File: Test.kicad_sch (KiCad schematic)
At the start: 17 parts, among them Q1 DMTH10H015LK3-13, U1 ${SIM.PARAMS}

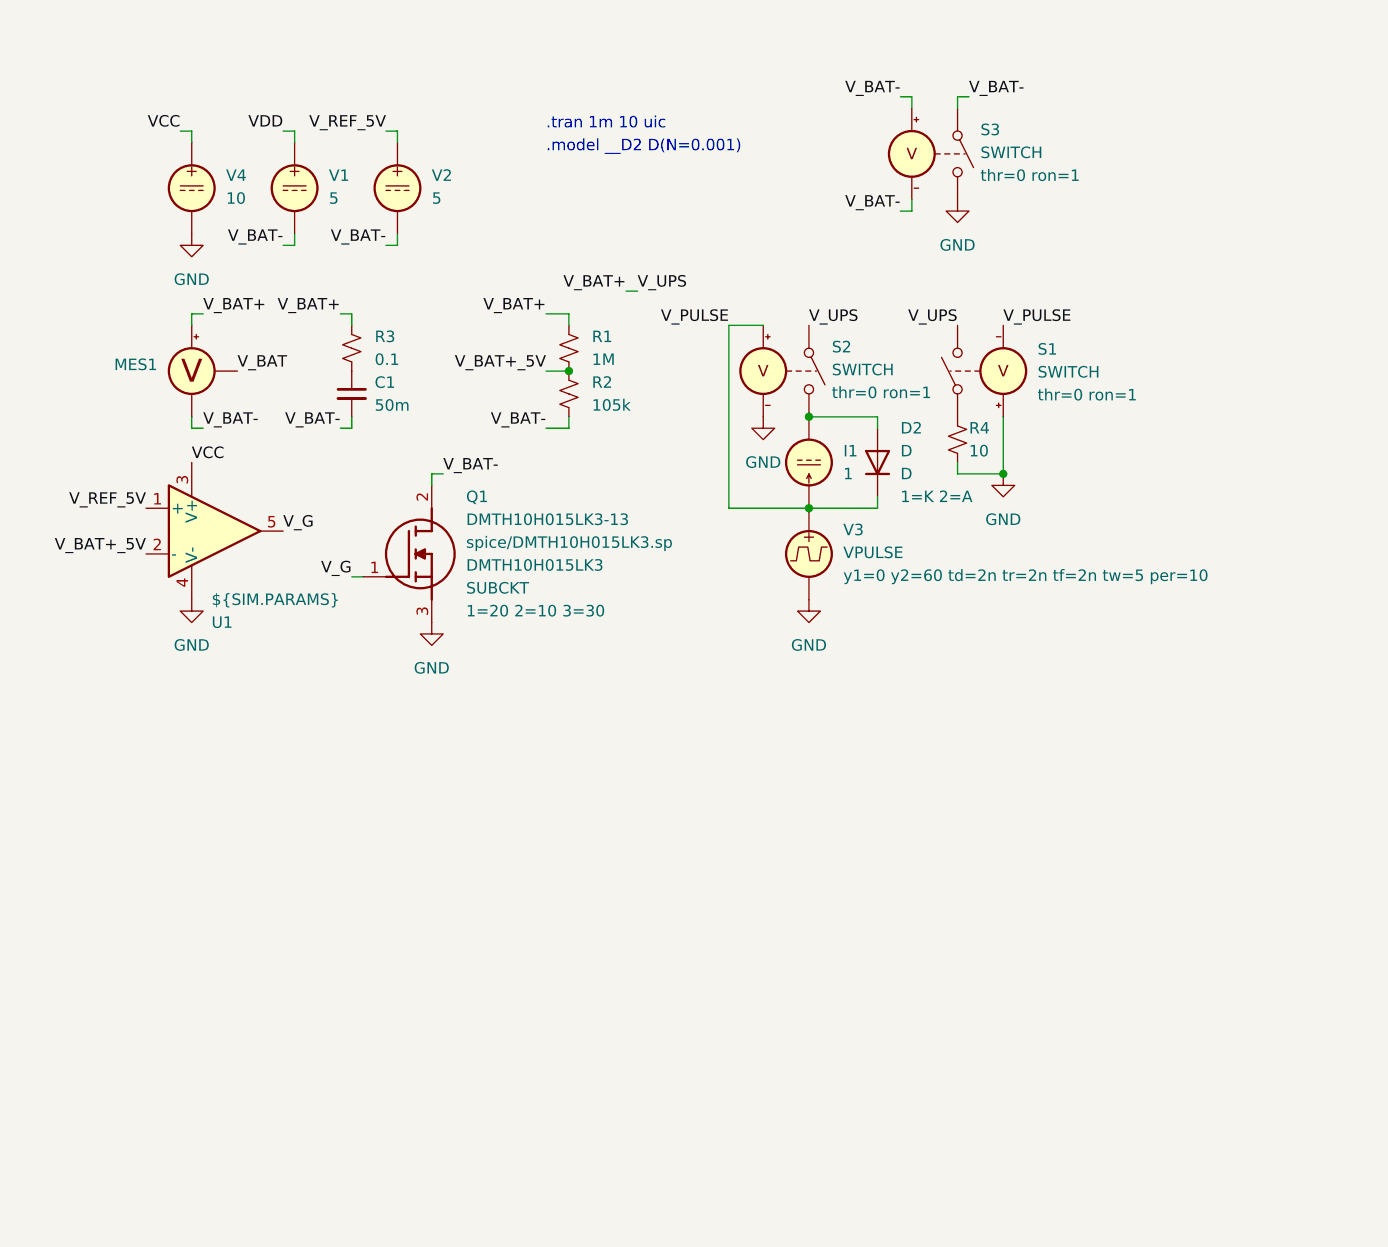
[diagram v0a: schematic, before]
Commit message: Replace simulation opamp with TL084HIDYYR
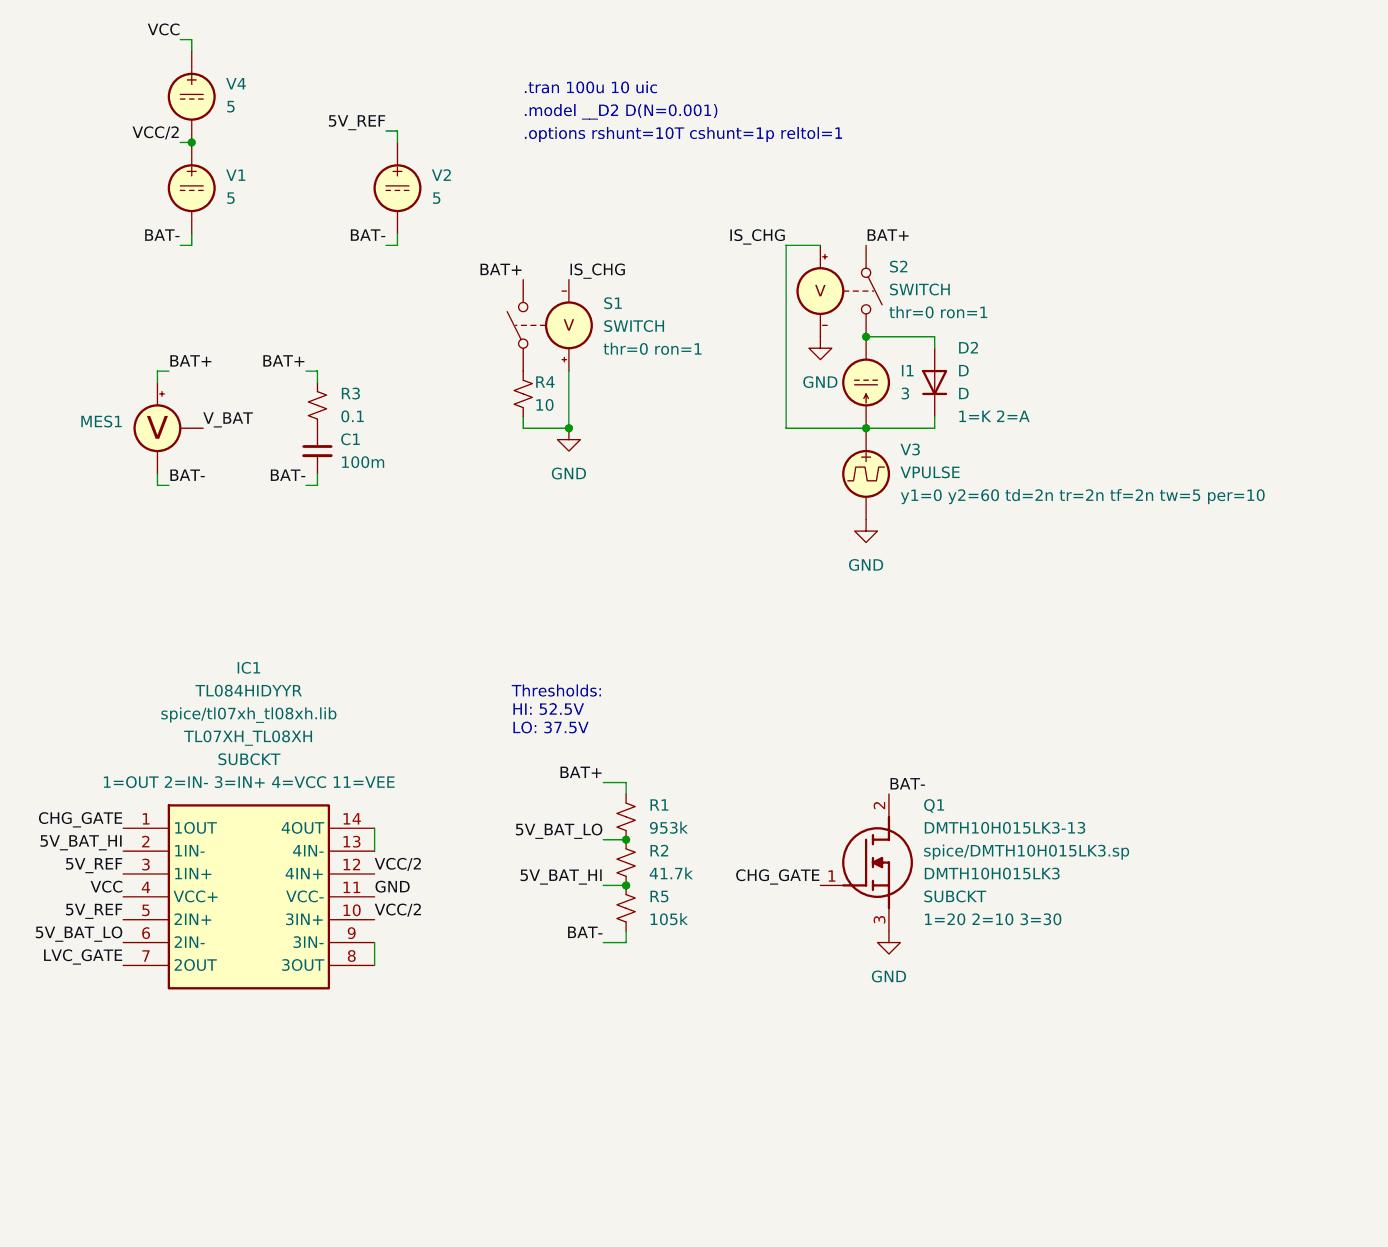
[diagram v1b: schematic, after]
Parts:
- removed S3: SWITCH, symbol Simulation_SPICE:SWITCH
- removed U1: ${SIM.PARAMS}, symbol Simulation_SPICE:OPAMP
- added IC1: TL084HIDYYR, SOP50P326X110-14N, symbol TL084HIDYYR:TL084HIDYYR
- added R5: 105k, symbol Device:R_Small_US
- C1: value 50m -> 100m
- I1: value 1 -> 3
- R1: value 1M -> 953k
- R2: value 105k -> 41.7k
- V4: value 10 -> 5
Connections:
- net GND: now also IC1.11 (VCC-); no longer V4.2
- net VCC: now also IC1.4 (VCC+)
- net VDD renamed VCC/2
- net VCC/2: now also V4.2, IC1.10 (3IN+), IC1.12 (4IN+)
- net V_BAT+ renamed BAT+
- net V_BAT+_5V renamed 5V_BAT_LO
- net 5V_BAT_LO: now also IC1.6 (2IN-)
- net V_BAT- renamed BAT-
- net BAT-: now also R5.1; no longer R2.1
- net V_G renamed CHG_GATE
- net CHG_GATE: now also IC1.1 (1OUT)
- net V_PULSE renamed IS_CHG
- net V_REF_5V renamed 5V_REF
- net 5V_REF: now also IC1.3 (1IN+), IC1.5 (2IN+)
- new net: IC1.13 (4IN-), IC1.14 (4OUT)
- new net: IC1.8 (3OUT), IC1.9 (3IN-)
- new net 5V_BAT_HI: IC1.2 (1IN-), R2.1, R5.2
- new net LVC_GATE: IC1.7 (2OUT)
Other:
- note added: ".options rshunt=10T cshunt=1p reltol=1"
- note added: ".tran 100u 10 uic"
- note added: "Thresholds: HI: 52.5V LO: 37.5V"
- note removed: ".tran 1m 10 uic"
- moved on the sheet: C1, D2, I1, MES1, Q1, R1, R2, R3, R4, S1, S2, V3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

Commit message: Replace simulation vref with LM4040CIM3-5.0+T
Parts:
- removed V2, V4: 5, symbol Simulation_SPICE:VDC
- added IC2: LM4040CIM3-5.0+T, SOT95P237X112-3N, symbol LM4040CIM3-5_0+T:LM4040CIM3-5.0+T
- added R6: 10k, symbol Device:R_Small_US
- C1: value 100m -> 150m
- V1: value 5 -> 10
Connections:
- net VCC/2 is gone; now on net VCC: IC1.10 (3IN+), IC1.12 (4IN+), V1.1
- net 5V_REF: now also IC2.1 (+), R6.1
- net BAT-: now also IC2.2 (-)
- net VCC: now also R6.2
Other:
- note added: ".tran 1m 10 uic"
- note removed: ".tran 100u 10 uic"
